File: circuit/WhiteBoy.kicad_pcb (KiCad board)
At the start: 2 copper layers, 100 x 100 mm, 100 parts, among them J1 HOLE, J2 HOLE, J3 HOLE, J4 HOLE, Q1 IRF530NPbF, Q2 BC547, Q3 BC557, Q4 BC547, T1 PB0, T2 PB1, T3 PB2, T4 PC1, T5 PC3, T6 PD6, T7 PD7, U1 74AC164, U10 74AC164, U11 CSR8635_MODULE, U12 TPA3136D2, U13 CSR_DebugSmall, U2 DS18B20, U3 MAX6457, U4 INA219_SOIC, U5 AVR-ISP6, U6 ATMEGA8-16AU, U7 74AC164, U8 DBG, U9 LM2576T-ADJ, Y1 16MHz

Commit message: i think this is done
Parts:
- added C24: 1uF, NovaBox:C_1206, F.Cu at (125.9, 88.9)
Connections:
- J1 pad 1: (no net) -> Net-(J1-Pad1)
- J2 pad 1: (no net) -> Net-(J2-Pad1)
- J3 pad 1: (no net) -> Net-(J3-Pad1)
- J4 pad 1: (no net) -> Net-(J4-Pad1)
- U11 pad 1: (no net) -> Net-(U11-Pad1)
- U11 pad 11: (no net) -> Net-(U11-Pad11)
- U11 pad 12: (no net) -> Net-(U11-Pad12)
- U11 pad 13: (no net) -> Net-(U11-Pad13)
- U11 pad 14: (no net) -> Net-(U11-Pad14)
- U11 pad 15: (no net) -> Net-(U11-Pad15)
- U11 pad 18: (no net) -> Net-(U11-Pad18)
- U11 pad 19: (no net) -> Net-(U11-Pad19)
- U11 pad 2: (no net) -> Net-(U11-Pad2)
- U11 pad 25: (no net) -> Net-(U11-Pad25)
- U11 pad 3: (no net) -> Net-(U11-Pad3)
- U11 pad 31: (no net) -> Net-(U11-Pad31)
- U11 pad 32: (no net) -> Net-(U11-Pad32)
- U11 pad 33: (no net) -> Net-(U11-Pad33)
- U11 pad 34: (no net) -> Net-(U11-Pad34)
- U11 pad 35: (no net) -> Net-(U11-Pad35)
- U11 pad 38: (no net) -> Net-(U11-Pad38)
- U11 pad 39: (no net) -> Net-(U11-Pad39)
- U11 pad 4: (no net) -> Net-(U11-Pad4)
- U11 pad 6: (no net) -> Net-(U11-Pad6)
- U11 pad 7: (no net) -> Net-(U11-Pad7)
- U11 pad 8: (no net) -> Net-(U11-Pad8)
- U11 pad 9: (no net) -> Net-(U11-Pad9)
- U12 pad 13: (no net) -> Net-(U12-Pad13)
- U12 pad 3: (no net) -> Net-(U12-Pad3)
- U12 pad 4: (no net) -> Net-(U12-Pad4)
- U12 pad 5: (no net) -> Net-(U12-Pad5)
- U12 pad 6: (no net) -> Net-(U12-Pad6)
- U6 pad 19: (no net) -> Net-(U6-Pad19)
- U6 pad 2: (no net) -> Net-(U6-Pad2)
- U6 pad 22: (no net) -> Net-(U6-Pad22)
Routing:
- net +4V: track 282.0 -> 285.0 mm
- net LED_RST: track 61.6 -> 64.2 mm

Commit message: sent to DirtyPCB!
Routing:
- net GND: track 19.8 -> 9.71 mm
- net +4V: track 285.0 -> 282.9 mm
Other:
- board text added: "https://github.com/nodep/NovaBox/ 2018.dec.10"
- board text removed: "https://github.com/nodep/NovaBox/ 2018.dec.9"

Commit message: calcVoltage can calc MAX6457 resistors; changed the schematic and PCB to include the resistor values
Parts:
- R10: value R -> 121K
- R11: value R -> 90K9
- R6: value R -> 750K
- RN1, RN2, RN3, RN4, RN5, RN6: value 150R -> 100R
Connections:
- J1 pad 1: Net-(J1-Pad1) -> (no net)
- J2 pad 1: Net-(J2-Pad1) -> (no net)
- J3 pad 1: Net-(J3-Pad1) -> (no net)
- J4 pad 1: Net-(J4-Pad1) -> (no net)
- U11 pad 1: Net-(U11-Pad1) -> (no net)
- U11 pad 11: Net-(U11-Pad11) -> (no net)
- U11 pad 12: Net-(U11-Pad12) -> (no net)
- U11 pad 13: Net-(U11-Pad13) -> (no net)
- U11 pad 14: Net-(U11-Pad14) -> (no net)
- U11 pad 15: Net-(U11-Pad15) -> (no net)
- U11 pad 18: Net-(U11-Pad18) -> (no net)
- U11 pad 19: Net-(U11-Pad19) -> (no net)
- U11 pad 2: Net-(U11-Pad2) -> (no net)
- U11 pad 25: Net-(U11-Pad25) -> (no net)
- U11 pad 3: Net-(U11-Pad3) -> (no net)
- U11 pad 31: Net-(U11-Pad31) -> (no net)
- U11 pad 32: Net-(U11-Pad32) -> (no net)
- U11 pad 33: Net-(U11-Pad33) -> (no net)
- U11 pad 34: Net-(U11-Pad34) -> (no net)
- U11 pad 35: Net-(U11-Pad35) -> (no net)
- U11 pad 38: Net-(U11-Pad38) -> (no net)
- U11 pad 39: Net-(U11-Pad39) -> (no net)
- U11 pad 4: Net-(U11-Pad4) -> (no net)
- U11 pad 6: Net-(U11-Pad6) -> (no net)
- U11 pad 7: Net-(U11-Pad7) -> (no net)
- U11 pad 8: Net-(U11-Pad8) -> (no net)
- U11 pad 9: Net-(U11-Pad9) -> (no net)
- U12 pad 13: Net-(U12-Pad13) -> (no net)
- U12 pad 3: Net-(U12-Pad3) -> (no net)
- U12 pad 4: Net-(U12-Pad4) -> (no net)
- U12 pad 5: Net-(U12-Pad5) -> (no net)
- U12 pad 6: Net-(U12-Pad6) -> (no net)
- U6 pad 19: Net-(U6-Pad19) -> (no net)
- U6 pad 2: Net-(U6-Pad2) -> (no net)
- U6 pad 22: Net-(U6-Pad22) -> (no net)

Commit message: changed resistor value
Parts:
- R10: value 121K -> 115K
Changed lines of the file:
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@@
       (effects (font (size 0.75 0.75) (thickness 0.15)))
     )
-    (fp_text value 121K (at -2.286 0) (layer F.Fab) hide
+    (fp_text value 115K (at -2.286 0) (layer F.Fab) hide
       (effects (font (size 0.127 0.127) (thickness 0.001)))
     )

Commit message: added changes to the PCB
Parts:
- removed R21: 100K, NovaBox:R_10MM
- removed R23: 10K, NovaBox:R_10MM
- removed RV1: 100K, NovaBox:RPOT_RKT6V
- added C25: 220μF, NovaBox:CPOL_D8_P3.5, F.Cu at (80.6, 138.4)
- added C26: 220μF, NovaBox:CPOL_D8_P3.5, F.Cu at (79.4, 108.0)
- added SW1: POS, NovaBox:SW_SPDT, F.Cu at (100.3, 125.6)
- added SW2: NEG, NovaBox:SW_SPDT, F.Cu at (104.1, 125.6)
- C16: footprint NovaBox:C_1206 -> NovaBox:CPOL_D4_P2
- R26: value 100K -> 10K
- R3: value 1K -> 2K7
- U6: value ATMEGA8-16AU -> ATMEGA88PA-16AU
- moved C21 4.44 mm to (89.3, 119.5)
- moved C20 4.44 mm to (89.3, 121.8)
- moved C14 2.93 mm to (89.3, 126.7)
- moved C11 2.59 mm to (77.9, 132.3)
- moved C8 2.39 mm to (77.9, 114.4)
- moved C15 2.10 mm to (89.3, 124.5)
- moved U13 2.07 mm to (121.0, 122.4)
- moved C12 1.90 mm to (77.9, 130.0)
- moved C9 1.70 mm to (77.9, 116.7)
- moved C13 1.61 mm to (61.3, 125.0)
- moved C19 1.60 mm to (61.3, 121.4), turned to 0 degrees
- moved C16 1.26 mm to (137.5, 146.0)
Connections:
- C14 pad 1: Net-(C14-Pad1) -> VDD
- C19 pad 1: GND -> Net-(C19-Pad1)
- C19 pad 2: Net-(C19-Pad2) -> GND
- C20 pad 2: SPK_RP -> BT_NEG
- C21 pad 2: SPK_RN -> BT_POS
- L3 pad 2: Net-(C19-Pad2) -> Net-(C19-Pad1)
- S2 pad 2: Net-(C19-Pad2) -> Net-(C19-Pad1)
- U11 pad 36: SPK_RN -> /SPK_RN
- U11 pad 37: SPK_RP -> /SPK_RP
- U11 pad 38: (no net) -> /SPK_LN
- U11 pad 39: (no net) -> /SPK_LP
- U12 pad 10: /PLIMIT -> /GVDD
- U12 pad 14: Net-(R21-Pad2) -> VDD
- U12 pad 7: Net-(C14-Pad1) -> VDD
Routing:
- net Net-(Q4-Pad1): track 57.0 -> 8.53 mm, vias 1 -> 0
- net SPK_RN: track 37.2 -> 0.00 mm
- net SPK_RP: track 36.7 -> 0.00 mm
- net /SPK_RP: track 0.00 -> 33.0 mm
- net /SPK_LP: track 0.00 -> 29.1 mm
- net /SPK_RN: track 0.00 -> 28.6 mm
- net /SPK_LN: track 0.00 -> 24.7 mm
- net /PLIMIT: track 21.8 -> 0.00 mm
- net /GVDD: track 27.6 -> 5.81 mm
- net Net-(C19-Pad2): track 16.7 -> 0.00 mm
- net BT_NEG: track 0.00 -> 15.9 mm
- net Net-(C19-Pad1): track 0.00 -> 15.0 mm
- net BT_POS: track 0.00 -> 11.9 mm
- net Net-(C14-Pad1): track 9.39 -> 0.00 mm
- net VDD: track 207.5 -> 199.4 mm
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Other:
- board text added: "https://github.com/nodep/NovaBox/ 2019.feb.10"
- board text added: "left"
- board text added: "right"
- board text removed: "https://github.com/nodep/NovaBox/ 2018.dec.10"

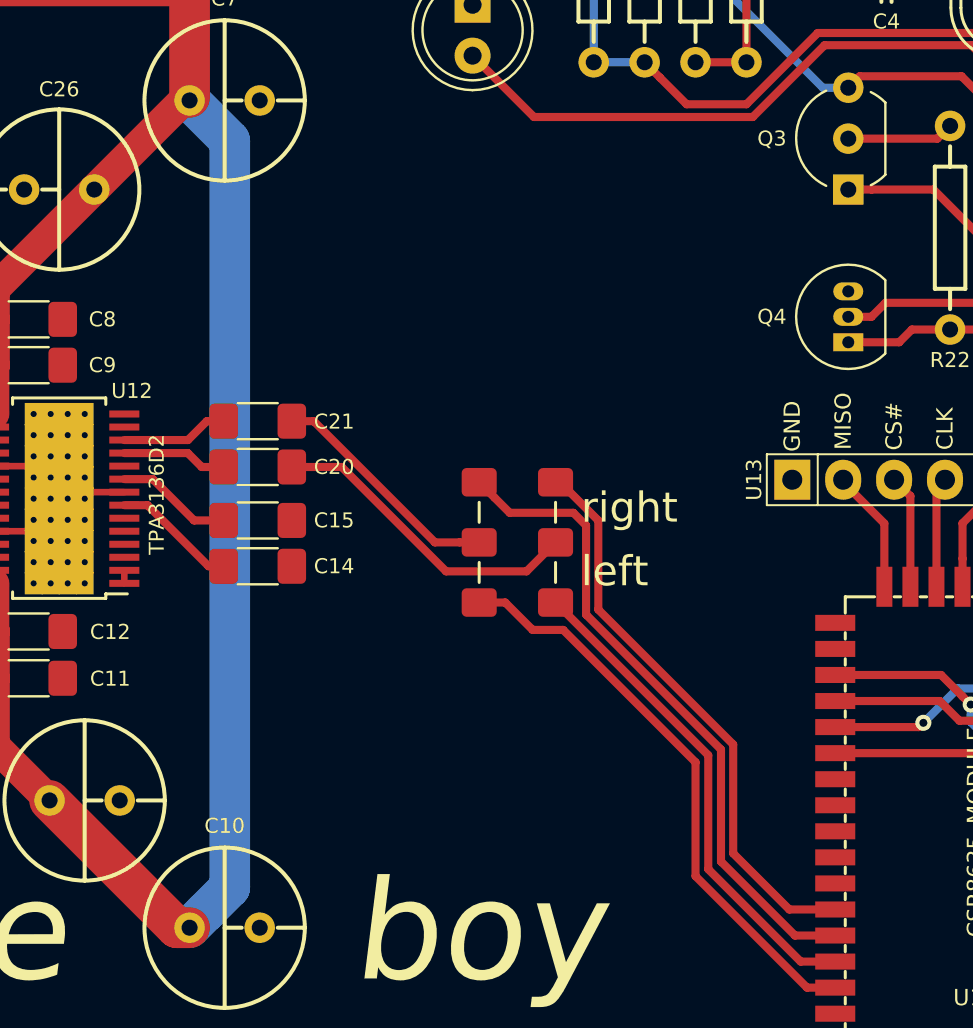
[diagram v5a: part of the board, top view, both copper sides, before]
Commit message: firmware shows power and voltage on the 7seg
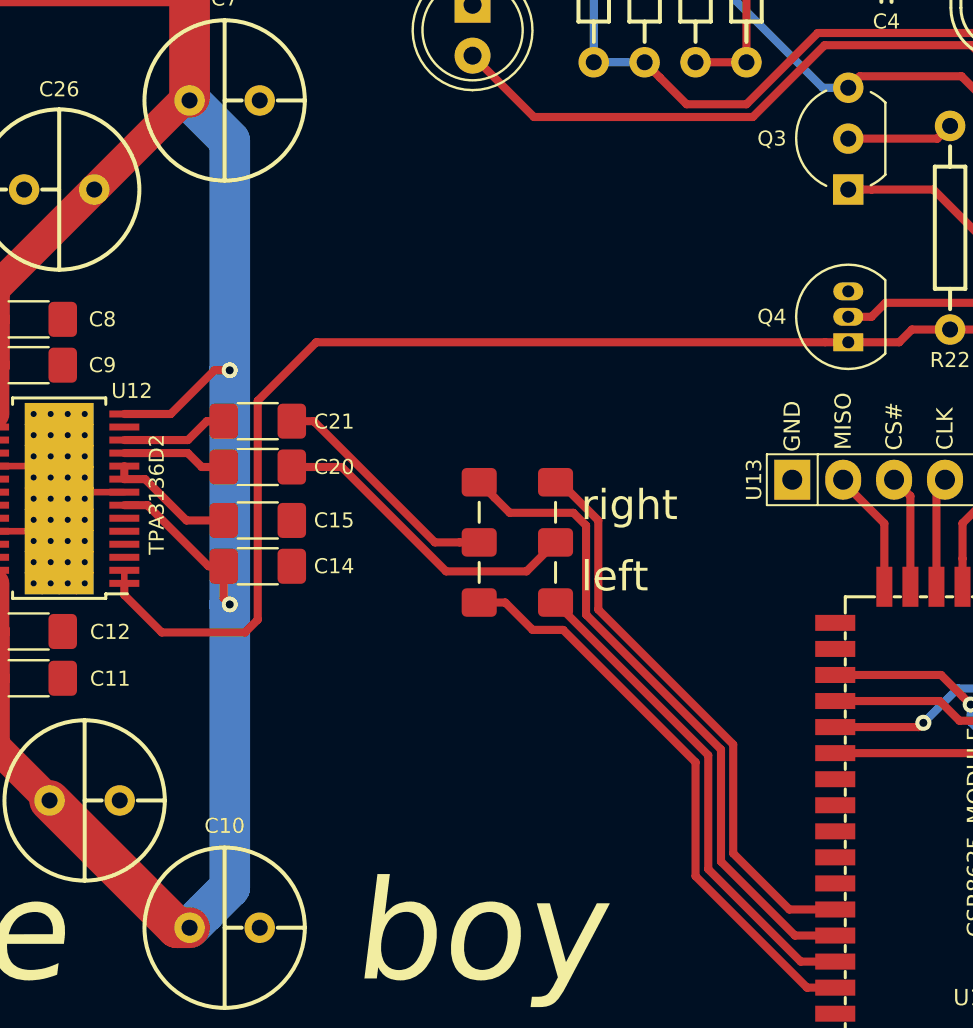
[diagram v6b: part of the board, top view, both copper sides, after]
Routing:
- net Net-(Q4-Pad1): track 8.53 -> 58.4 mm
- net VDD: track 199.4 -> 207.6 mm, vias 0 -> 2
- net /GVDD: track 5.81 -> 6.46 mm
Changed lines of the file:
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@@
     (thickness 1.6)
     (drawings 13)
-    (tracks 945)
+    (tracks 963)
     (zones 0)
     (modules 102)
@@
   )
   (setup
-    (last_trace_width 1.524)
+    (last_trace_width 0.2032)
     (user_trace_width 0.3302)
     (user_trace_width 0.4064)
@@
     )
   )
-  (gr_text left (at 105.41 127) (layer F.SilkS)
+  (gr_text left (at 105.41 127.254) (layer F.SilkS)
     (effects (font (size 1.5 1.5) (thickness 0.3)) (justify left))
   )
-  (gr_text right (at 105.41 123.825) (layer F.SilkS)
+  (gr_text right (at 105.41 123.698) (layer F.SilkS)
     (effects (font (size 1.5 1.5) (thickness 0.3)) (justify left))
   )
@@
   (segment (start 87.884 142.776) (end 86.641999 144.018001) (width 2.032) (layer B.Cu) (net 8))
   (segment (start 85.88 103.505) (end 87.884 105.509) (width 2.032) (layer B.Cu) (net 8) (status 10))
-  (segment (start 87.884 105.509) (end 87.884 142.776) (width 2.032) (layer B.Cu) (net 8))
   (segment (start 85.725 64.8586) (end 85.725 66.215) (width 0.4064) (layer F.Cu) (net 8) (status 20))
   (segment (start 84.3664 63.5) (end 85.725 64.8586) (width 0.4064) (layer F.Cu) (net 8))
@@
   (segment (start 76.151 112.924) (end 81.125 107.95) (width 1.524) (layer F.Cu) (net 8))
   (segment (start 76.151 114.427) (end 76.151 112.924) (width 1.524) (layer F.Cu) (net 8))
+  (via (at 87.884 128.651) (size 0.8) (drill 0.4) (layers F.Cu B.Cu) (net 8))
+  (segment (start 87.581 128.348) (end 87.884 128.651) (width 0.4064) (layer F.Cu) (net 8))
+  (segment (start 87.581 126.746) (end 87.581 128.348) (width 0.4064) (layer F.Cu) (net 8))
+  (segment (start 87.884 128.651) (end 87.884 142.776) (width 2.032) (layer B.Cu) (net 8))
+  (via (at 87.884 116.967) (size 0.8) (drill 0.4) (layers F.Cu B.Cu) (net 8))
+  (segment (start 87.884 105.509) (end 87.884 116.967) (width 2.032) (layer B.Cu) (net 8))
+  (segment (start 87.884 116.967) (end 87.884 128.651) (width 2.032) (layer B.Cu) (net 8))
+  (segment (start 87.122 116.967) (end 87.884 116.967) (width 0.4064) (layer F.Cu) (net 8))
+  (segment (start 82.625 119.148749) (end 84.940251 119.148749) (width 0.4064) (layer F.Cu) (net 8))
+  (segment (start 84.940251 119.148749) (end 87.122 116.967) (width 0.4064) (layer F.Cu) (net 8))
   (segment (start 53.715043 127.375043) (end 58.42 132.08) (width 2.032) (layer F.Cu) (net 9))
   (segment (start 53.715043 124.916249) (end 53.715043 127.375043) (width 2.032) (layer F.Cu) (net 9))
@@
   (segment (start 121.285 115.57) (end 121.92 114.935) (width 0.4064) (layer F.Cu) (net 26))
   (segment (start 82.625 126.948749) (end 82.625 127.598749) (width 0.3302) (layer F.Cu) (net 26) (status 30))
+  (segment (start 117.5886 115.57) (end 118.745 115.57) (width 0.4064) (layer F.Cu) (net 26))
+  (segment (start 92.202 115.57) (end 117.5886 115.57) (width 0.4064) (layer F.Cu) (net 26))
+  (segment (start 82.625 128.180149) (end 84.492851 130.048) (width 0.4064) (layer F.Cu) (net 26))
+  (segment (start 82.625 127.598749) (end 82.625 128.180149) (width 0.4064) (layer F.Cu) (net 26))
+  (segment (start 84.492851 130.048) (end 88.646 130.048) (width 0.4064) (layer F.Cu) (net 26))
+  (segment (start 88.646 130.048) (end 89.281 129.413) (width 0.4064) (layer F.Cu) (net 26))
+  (segment (start 89.281 129.413) (end 89.281 118.491) (width 0.4064) (layer F.Cu) (net 26))
+  (segment (start 89.281 118.491) (end 92.202 115.57) (width 0.4064) (layer F.Cu) (net 26))
   (segment (start 134.62 82.55) (end 134.62 85.09) (width 0.4064) (layer F.Cu) (net 27) (status 20))
   (segment (start 136.525 80.645) (end 134.62 82.55) (width 0.4064) (layer F.Cu) (net 27))
@@
   (segment (start 132.2705 102.6795) (end 133.223 101.727) (width 0.4064) (layer F.Cu) (net 109) (status 10))
   (segment (start 133.223 101.727) (end 133.223 100.33) (width 0.4064) (layer F.Cu) (net 109))
-  (segment (start 86.106 124.46) (end 87.581 124.46) (width 0.4064) (layer F.Cu) (net 110))
-  (segment (start 82.625 122.398749) (end 84.044749 122.398749) (width 0.4064) (layer F.Cu) (net 110))
-  (segment (start 84.044749 122.398749) (end 86.106 124.46) (width 0.4064) (layer F.Cu) (net 110))
+  (segment (start 82.625 121.748749) (end 82.625 122.398749) (width 0.4064) (layer F.Cu) (net 110))
+  (segment (start 85.725 124.46) (end 87.581 124.46) (width 0.4064) (layer F.Cu) (net 110))
+  (segment (start 82.625 122.398749) (end 83.663749 122.398749) (width 0.4064) (layer F.Cu) (net 110))
+  (segment (start 83.663749 122.398749) (end 85.725 124.46) (width 0.4064) (layer F.Cu) (net 110))
   (segment (start 53.715043 119.004957) (end 58.42 114.3) (width 2.032) (layer F.Cu) (net 111))
   (segment (start 53.715043 121.416249) (end 53.715043 119.004957) (width 2.032) (layer F.Cu) (net 111))
@@
   (segment (start 90.981 121.793) (end 93.472 121.793) (width 0.4064) (layer F.Cu) (net 113))
   (segment (start 93.472 121.793) (end 98.679 127) (width 0.4064) (layer F.Cu) (net 113))
-  (segment (start 101.631 128.555) (end 100.33 128.555) (width 0.4064) (layer F.Cu) (net 115))
-  (segment (start 116.6886 147.77) (end 111.125 142.2064) (width 0.4064) (layer F.Cu) (net 115))
-  (segment (start 118.095 147.77) (end 116.6886 147.77) (width 0.4064) (layer F.Cu) (net 115))
-  (segment (start 111.125 136.525) (end 104.521 129.921) (width 0.4064) (layer F.Cu) (net 115))
-  (segment (start 111.125 142.2064) (end 111.125 136.525) (width 0.4064) (layer F.Cu) (net 115))
-  (segment (start 104.521 129.921) (end 102.997 129.921) (width 0.4064) (layer F.Cu) (net 115))
-  (segment (start 102.997 129.921) (end 101.631 128.555) (width 0.4064) (layer F.Cu) (net 115))
   (segment (start 101.854 124.079) (end 101.101484 123.326484) (width 0.4064) (layer F.Cu) (net 114))
   (segment (start 105.029 124.079) (end 101.854 124.079) (width 0.4064) (layer F.Cu) (net 114))
@@
   (segment (start 105.664 129.159) (end 105.664 124.714) (width 0.4064) (layer F.Cu) (net 114))
   (segment (start 105.664 124.714) (end 105.029 124.079) (width 0.4064) (layer F.Cu) (net 114))
+  (segment (start 101.631 128.555) (end 100.33 128.555) (width 0.4064) (layer F.Cu) (net 115))
+  (segment (start 116.6886 147.77) (end 111.125 142.2064) (width 0.4064) (layer F.Cu) (net 115))
+  (segment (start 118.095 147.77) (end 116.6886 147.77) (width 0.4064) (layer F.Cu) (net 115))
+  (segment (start 111.125 136.525) (end 104.521 129.921) (width 0.4064) (layer F.Cu) (net 115))
+  (segment (start 111.125 142.2064) (end 111.125 136.525) (width 0.4064) (layer F.Cu) (net 115))
+  (segment (start 104.521 129.921) (end 102.997 129.921) (width 0.4064) (layer F.Cu) (net 115))
+  (segment (start 102.997 129.921) (end 101.631 128.555) (width 0.4064) (layer F.Cu) (net 115))
   (segment (start 115.803 143.87) (end 118.095 143.87) (width 0.4064) (layer F.Cu) (net 116))
   (segment (start 104.367118 122.555) (end 106.27361 124.461492) (width 0.4064) (layer F.Cu) (net 116))
